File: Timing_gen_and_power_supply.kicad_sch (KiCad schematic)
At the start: 33 parts, among them Q1 LM340T5, Q2 LM340T12, Q3 2N3646, Q4 2N4916, Q5 2N3646, Q6 2N4916, U11 74LS10, U14 74LS109, U15 74LS20, U16 74LS04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

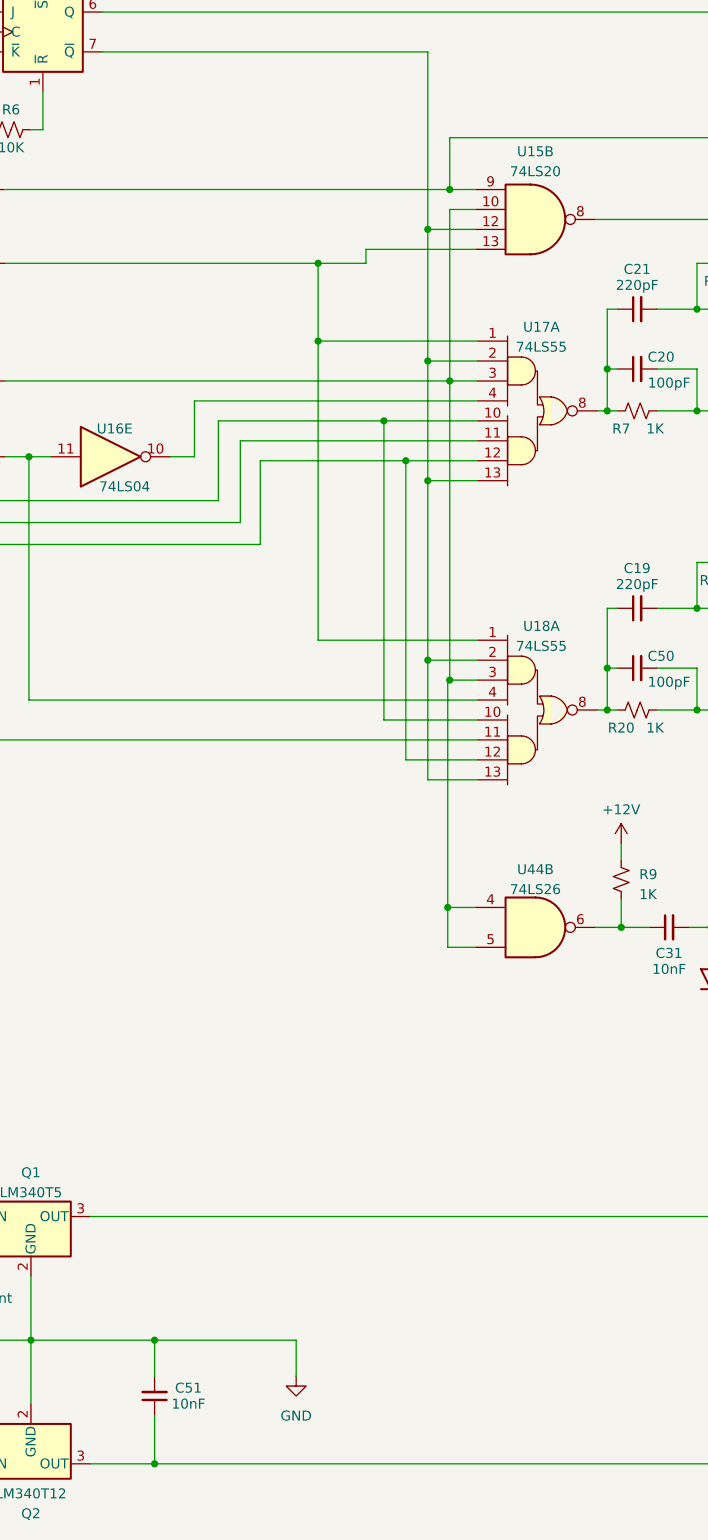
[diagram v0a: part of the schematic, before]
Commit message: Various corrections. Add new symbols and footprints
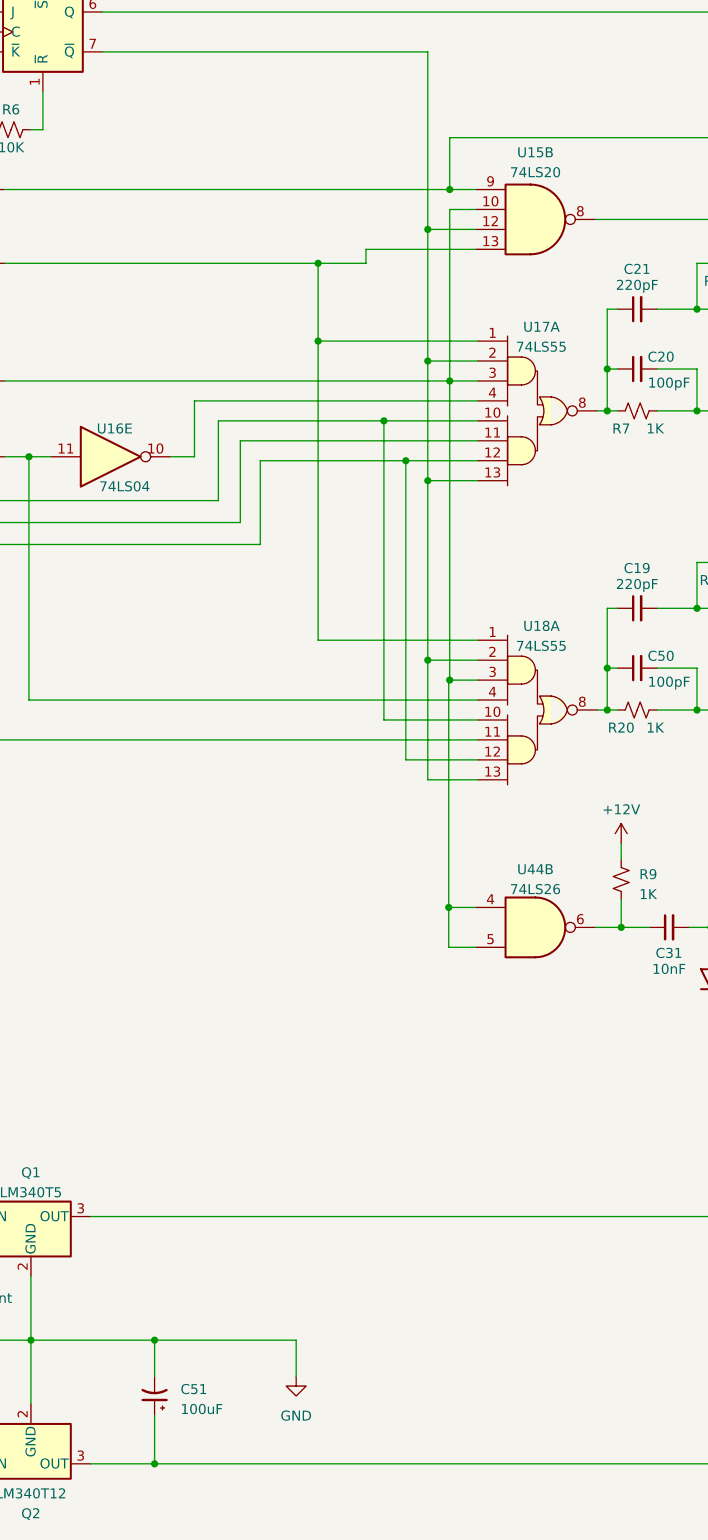
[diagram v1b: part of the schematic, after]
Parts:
- removed C51: 10nF, symbol Device:C_Small
- removed U15: 74LS20, symbol 74xx:74LS20
- added C51: 100uF, K-1008:CP_Radial_D10.0mm_P5.00mm, symbol Device:C_Polarized_Small_US
- added U15: 74LS20, symbol K-1008_Library:74LS20
- C1: footprint (none) -> K-1008:CP_Radial_D16.0mm_P6.35mm
- C19, C20, C21, C31, C50: footprint (none) -> K-1008:C_Disc_D8.0mm_W2.5mm_P6.35mm
- C2: footprint (none) -> K-1008:CP_Radial_Tantal_D4.5mm_P8.89mm
- C55: footprint (none) -> K-1008:CP_Radial_D10.0mm_P5.00mm
- D2, D3: footprint Diode_THT:D_DO-35_SOD27_P7.62mm_Horizontal -> K-1008:D_DO-35_SOD27_P12.70mm_Horizontal
- D4: footprint (none) -> K-1008:D_DO-35_SOD27_P12.70mm_Horizontal
- Q1, Q2: footprint (none) -> K-1008:TO-220-3_Horizontal_TabDown
- Q3, Q4, Q5, Q6: footprint Package_TO_SOT_THT:TO-92_Inline -> K-1008:TO-92
- R19, R8: footprint (none) -> K-1008:R_Axial_DIN0309_2K2_L6.3mm_D2.3mm_P12.70mm_Horizontal
- R20, R7, R9: footprint (none) -> K-1008:R_Axial_DIN0309_1K_L6.3mm_D2.3mm_P12.70mm_Horizontal
- R6: footprint (none) -> K-1008:R_Axial_DIN0309_10K_L6.3mm_D2.3mm_P12.70mm_Horizontal
- U11, U16, U4, U44, U6: footprint (none) -> K-1008:DIP-14_W7.62mm_LongPads
- U14: footprint (none) -> K-1008:DIP-16_W7.62mm_LongPads
- U17, U18: footprint (none) -> K-1008:DIP-14_W7.62mm_LongPads; symbol 74xx:74LS55 -> K-1008_Library:74LS55
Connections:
- net +12V: now also C51.1
- net GND: now also C51.2
- net ~{LOC_RW}: now also U15.9
- net ~{RAM_WE}: now also U15.8
- net at U16.2, U17.1, U18.1: now also U15.13
- net at U16.12, U17.3, U18.3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: now also U15.10
- net at U14.7 (~{Q}), U17.13, U17.2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: now also U15.12

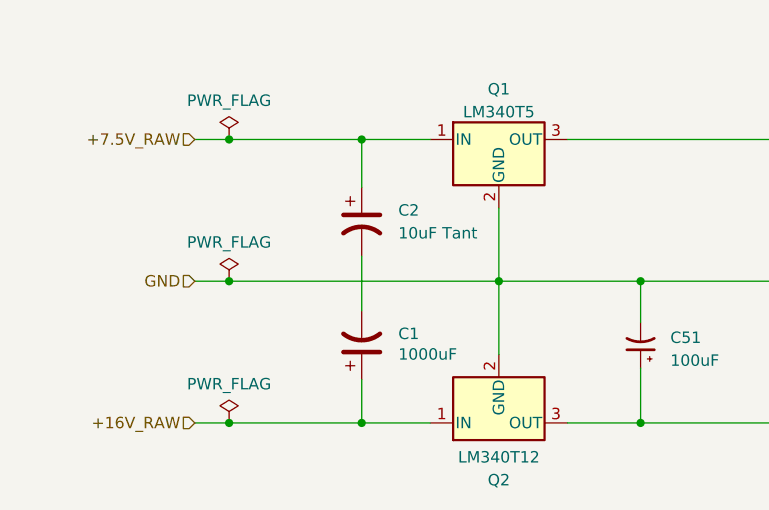
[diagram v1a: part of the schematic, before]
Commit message: Fix C1/C2 not connected to GND
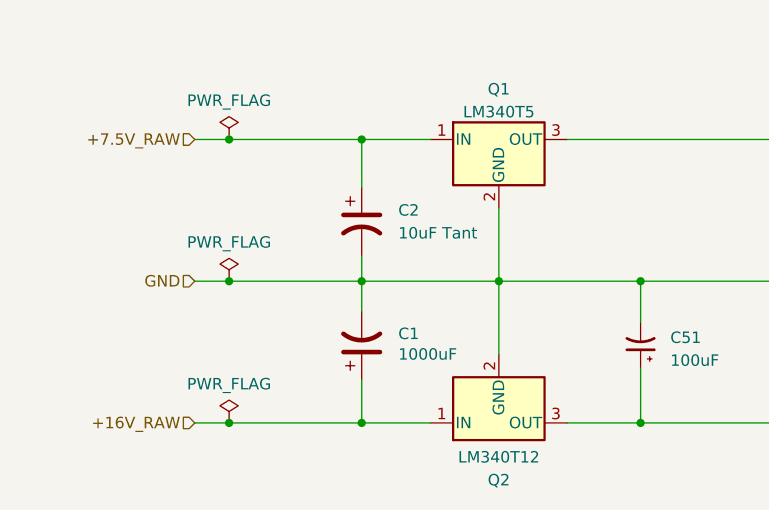
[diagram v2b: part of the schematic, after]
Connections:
- net GND: now also C1.2, C2.2
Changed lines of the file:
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@@
   (junction (at 162.306 124.968) (diameter 0) (color 0 0 0 0)
   )
+  (junction (at 50.8 211.836) (diameter 0) (color 0 0 0 0)
+  )
   (junction (at 116.586 87.122) (diameter 0) (color 0 0 0 0)
   )
@@
     (stroke (width 0) (type default))
   )
-  (wire (pts (xy 50.8 209.042) (xy 50.8 215.138))
+  (wire (pts (xy 50.8 209.042) (xy 50.8 211.836))
     (stroke (width 0) (type default))
   )
@@
     (stroke (width 0) (type default))
   )
+  (wire (pts (xy 50.8 211.836) (xy 50.8 215.138))
+    (stroke (width 0) (type default))
+  )
   (wire (pts (xy 32.004 89.662) (xy 43.688 89.662))
     (stroke (width 0) (type default))
@@
     (stroke (width 0) (type default))
   )
-  (wire (pts (xy 36.068 211.836) (xy 66.04 211.836))
+  (wire (pts (xy 36.068 211.836) (xy 50.8 211.836))
     (stroke (width 0) (type default))
   )
@@
     (stroke (width 0) (type default))
   )
+  (wire (pts (xy 50.8 211.836) (xy 66.04 211.836))
+    (stroke (width 0) (type default))
+  )

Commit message: Routing completed
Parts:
- added unit 4 of U15
- added unit 3 of U17
- added unit 3 of U18
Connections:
- net +12V: now also Q4.1 (E), Q6.1 (E); no longer Q4.3 (E), Q6.3 (E)
- net CE_EVEN: now also Q4.3 (C); no longer Q4.1 (C)
- net CE_ODD: now also Q6.3 (C); no longer Q6.1 (C)
- net HORIZ_UNBLK: now also U18.5 (N/C)
- net at U15.10, U16.12, U17.3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: now also U15.11 (N/C)
- net at U16.10, U17.4: now also U17.5 (N/C)
- no-connect marks 0 -> 5

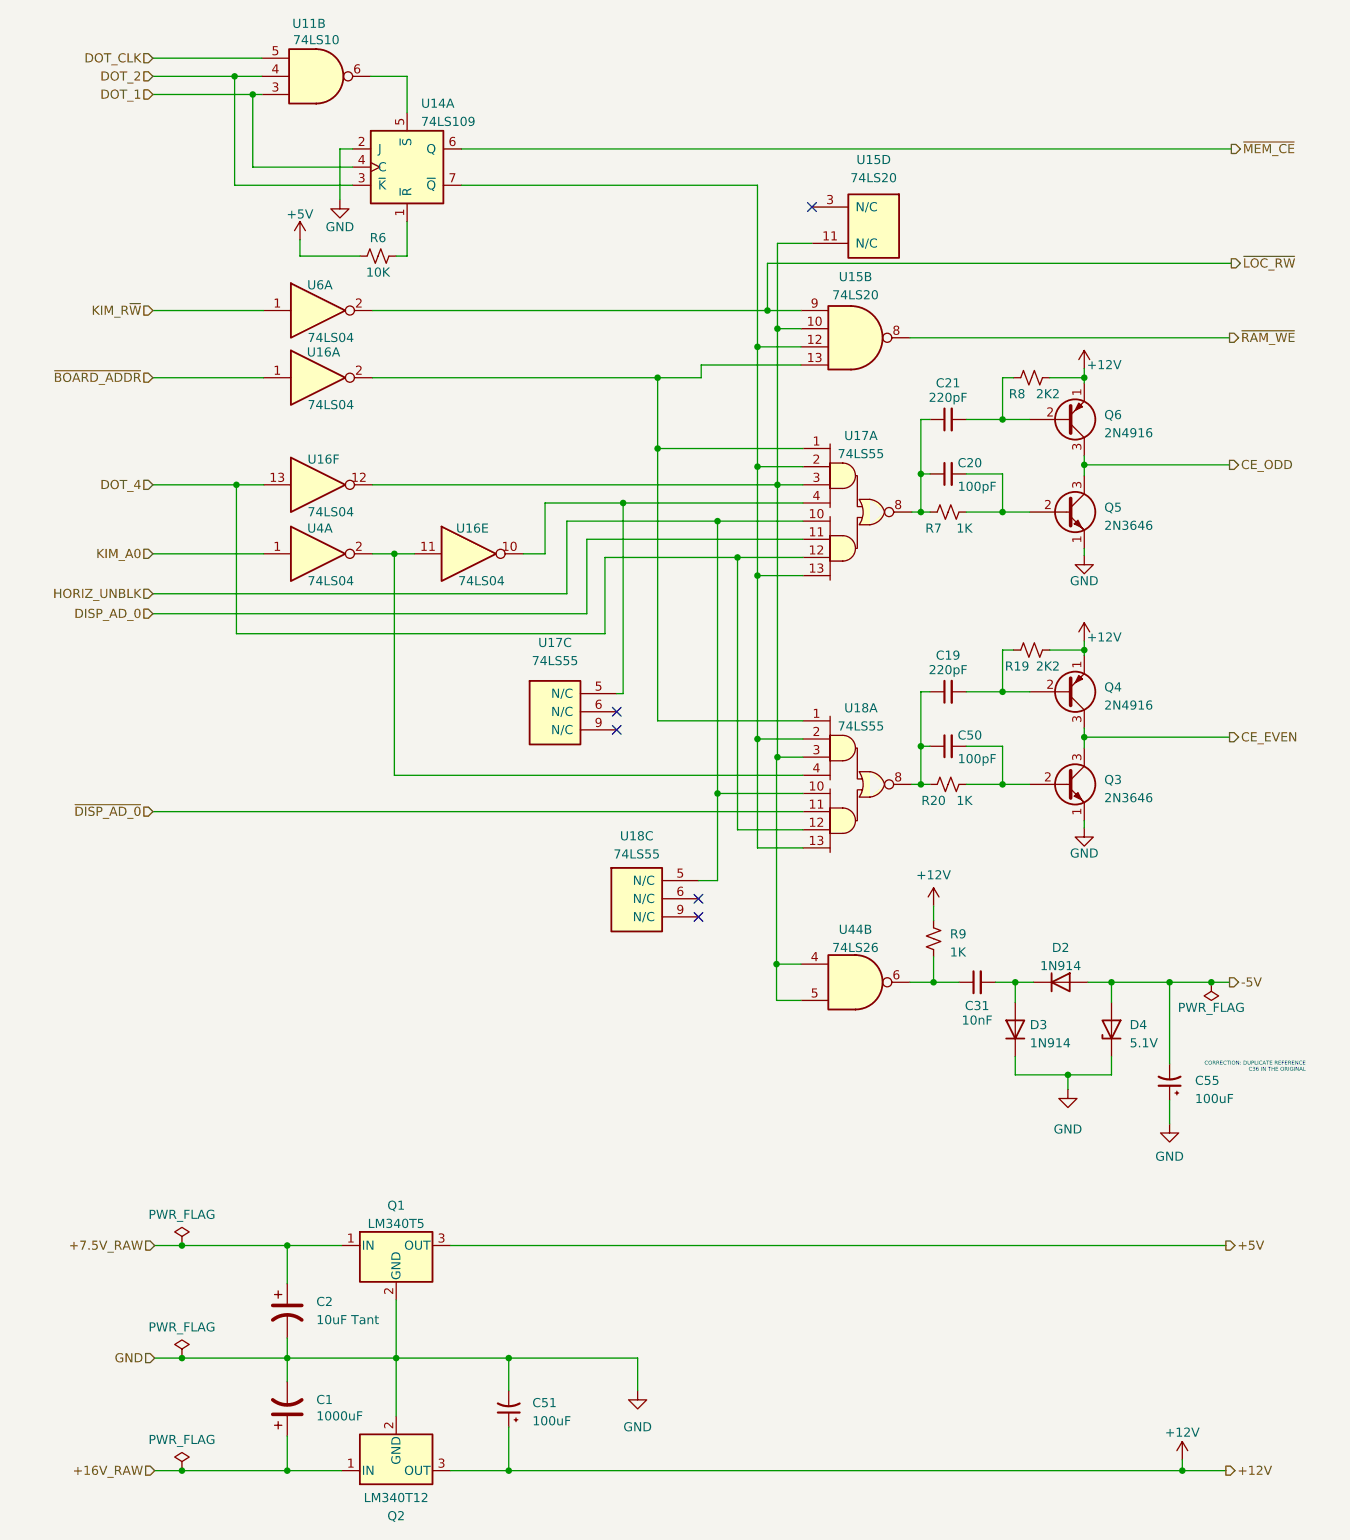
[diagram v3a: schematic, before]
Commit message: Add notes for obsolete parts and replacements
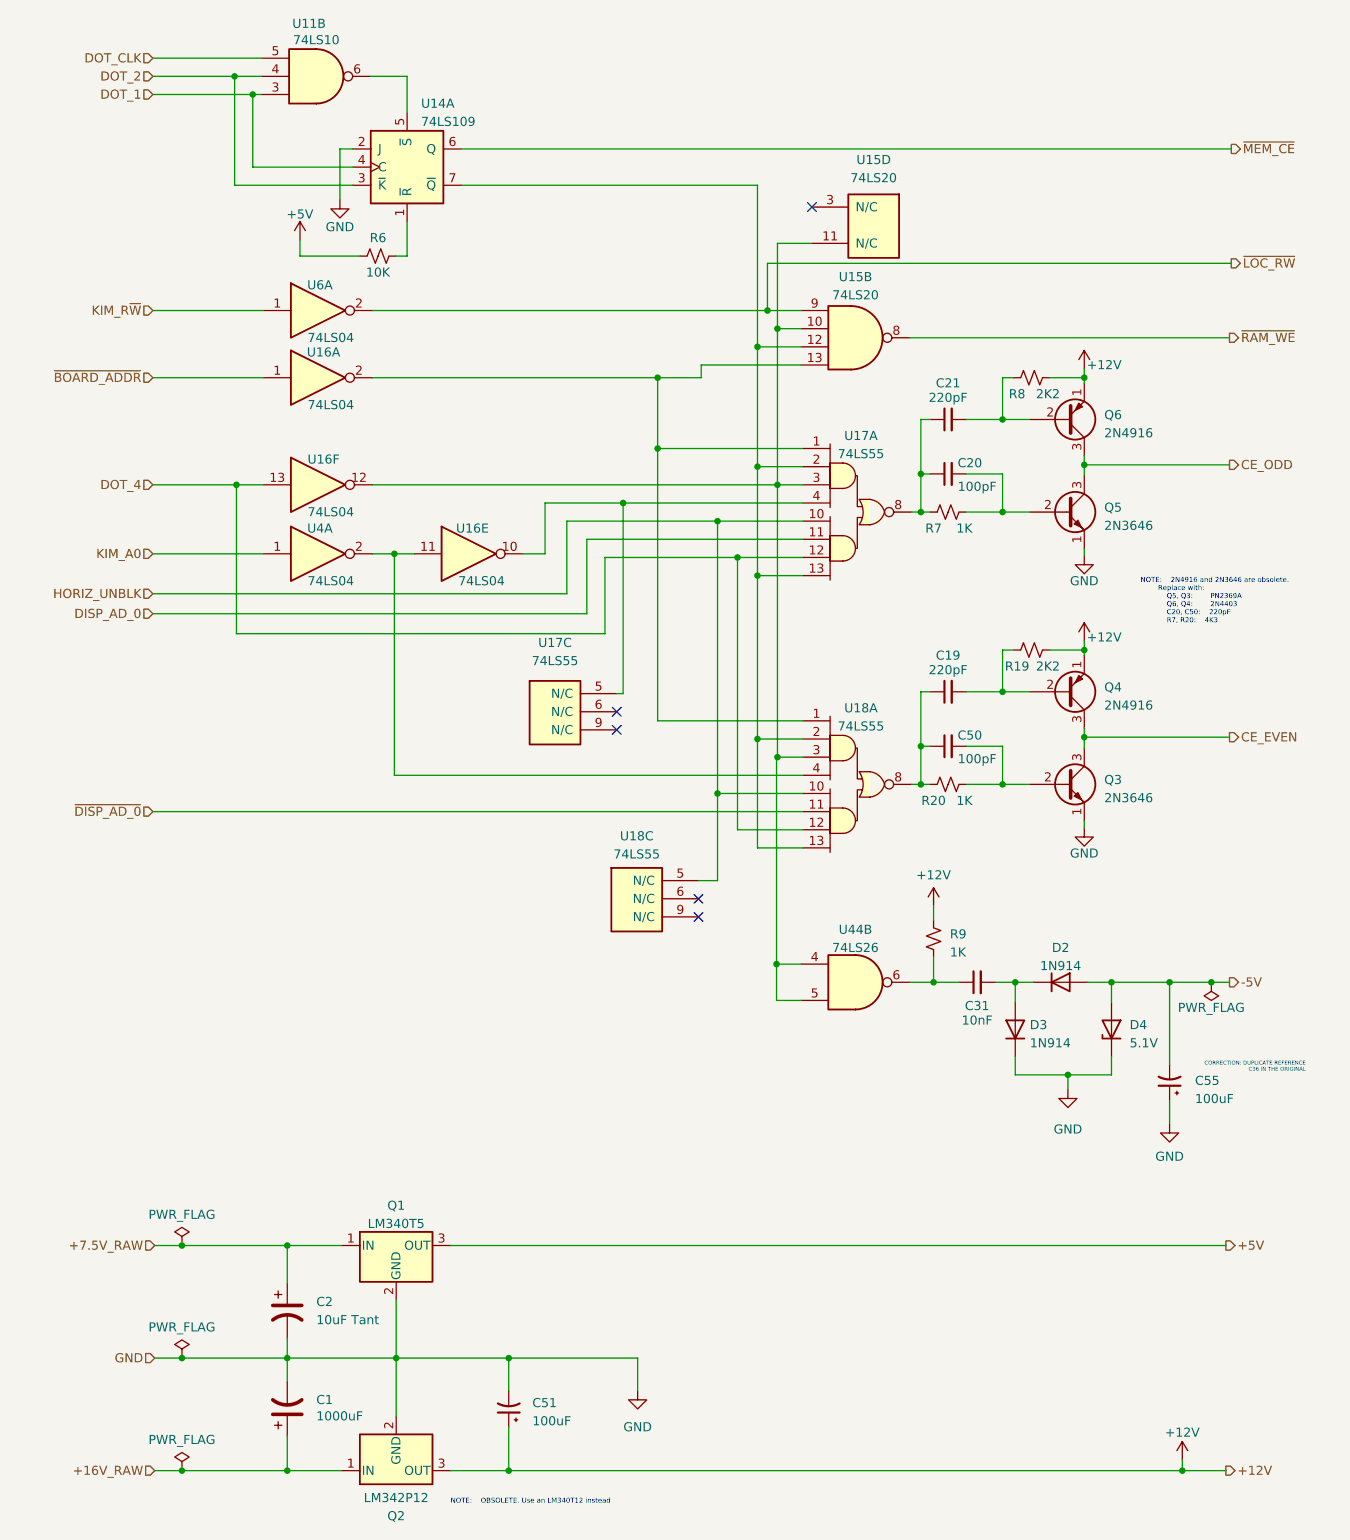
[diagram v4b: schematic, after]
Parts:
- Q2: value LM340T12 -> LM342P12
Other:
- note added: "NOTE: 2N4916 and 2N3646 are obsolete. Replace with: Q5, Q3: PN2369A Q6, Q4: 2N4403 C20, C50: 220pF R7, R20: 4K3"
- note added: "NOTE: OBSOLETE. Use an LM340T12 instead"
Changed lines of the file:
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@@
     (effects (font (size 0.54 0.54) (color 194 0 0 1)) (justify right bottom))
+  )
+  (text "NOTE:	OBSOLETE. Use an LM340T12 instead" (at 73.66 232.41 0)
+    (effects (font (size 0.7 0.7) (color 194 0 0 1)) (justify left bottom))
+  )
+  (text "NOTE:	2N4916 and 2N3646 are obsolete.\n		Replace with:\n			Q5, Q3:		PN2369A \n			Q6, Q4:		2N4403\n			C20, C50:	220pF\n			R7, R20:	4K3"
+    (at 170.18 109.22 0)
+    (effects (font (size 0.7 0.7) (color 194 0 0 1)) (justify left bottom))
   )
   (hierarchical_label "DISP_AD_0" (shape input) (at 32.004 107.696 180) (fields_autoplaced)
@@
       (effects (font (size 1.27 1.27)))
     )
-    (property "Value" "LM340T12" (at 66.04 231.394 0)
-      (effects (font (size 1.27 1.27)))
-    )
+    (property "Value" "LM342P12 " (at 66.04 231.394 0)
+      (effects (font (size 1.27 1.27)))
+    )
